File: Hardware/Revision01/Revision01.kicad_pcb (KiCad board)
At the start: 4 copper layers, 100 x 119.8 mm, 83 parts, among them J1 Battery connector, J2 StrainConn, J3 StrainConn, J4 StrainConn, J5 StrainConn, J6 StrainConn, J7 StrainConn, J8 StrainConn, J9 StrainConn, Q1 PMOS, Q2 NMOS, Q3 PMOS, SW1 StartStop_Push, SW2 ON/OFF_SW_SPST_LED, U1 NCP1117LPST50T3G, U2 NUCLEO-L476RG, U3 LP5813BDRRR, U4 MRF89XAM9AT-I/RM, U5 ICM-45605

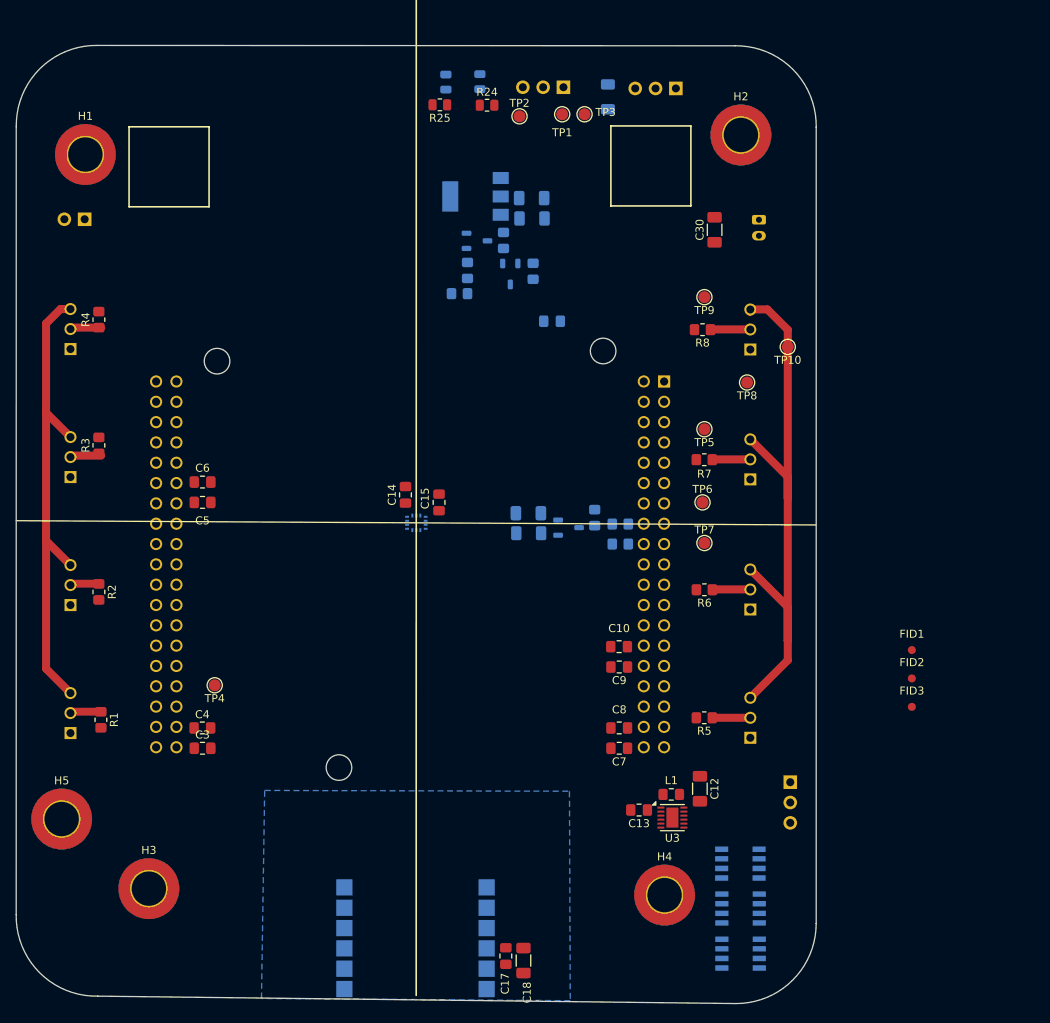
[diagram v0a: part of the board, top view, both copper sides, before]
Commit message: Added protection ciruitry and completed most of LAYOUT for PART A
 - Added SC protection against AMPLIFIER input circuitry
 -Completed PCB layout for STRAIN AMPLIFIER V1
 -Internal temperature sensor exists inside STM32
 -added schottky diodes to clamp over/undervoltage to protect ADC
 - Analog layer layout complete
 - Power circuitry layed out

Antenna has not been wired out
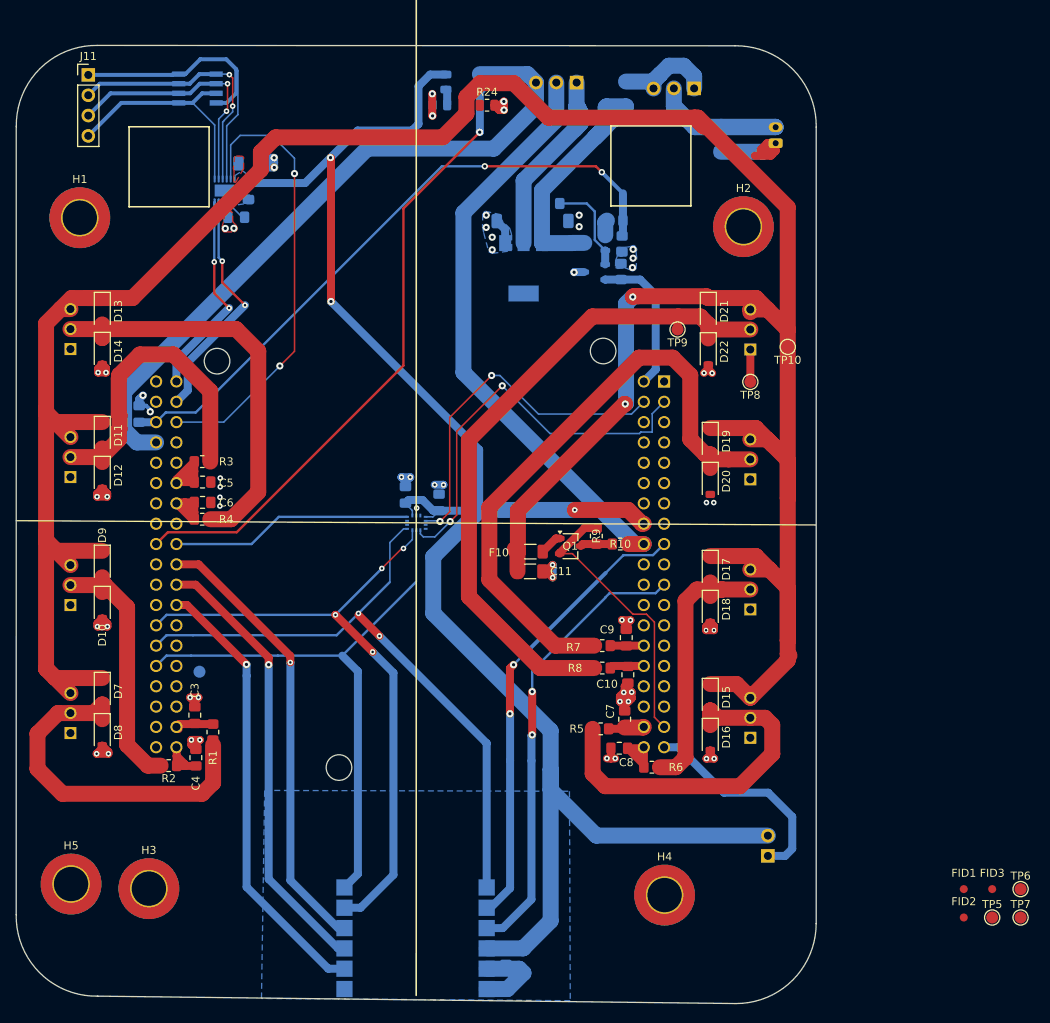
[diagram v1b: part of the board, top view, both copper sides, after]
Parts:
- removed D1: Indicication_RGB_Led, Connector_PinHeader_2.54mm:PinHeader_1x03_P2.54mm_Vertical
- removed D3, D4: RGBW_LED, RGBW:SOL120P540X160-8N
- removed R11: 0K +-1%, Resistor_SMD:R_0805_2012Metric_Pad1.20x1.40mm_HandSolder
- added D10: D_Schottky_Small, Diode_SMD:D_SOD-123, F.Cu at (121.8, 102.9)
- added D11: D_Schottky_Small, Diode_SMD:D_SOD-123, F.Cu at (121.8, 81.7)
- added D12: D_Schottky_Small, Diode_SMD:D_SOD-123, F.Cu at (121.8, 86.7)
- added D13: D_Schottky_Small, Diode_SMD:D_SOD-123, F.Cu at (121.8, 66.2)
- added D14: D_Schottky_Small, Diode_SMD:D_SOD-123, F.Cu at (121.8, 71.2)
- added D15: D_Schottky_Small, Diode_SMD:D_SOD-123, F.Cu at (197.8, 114.4)
- added D16: D_Schottky_Small, Diode_SMD:D_SOD-123, F.Cu at (197.8, 119.4)
- added D17: D_Schottky_Small, Diode_SMD:D_SOD-123, F.Cu at (197.8, 98.4)
- added D18: D_Schottky_Small, Diode_SMD:D_SOD-123, F.Cu at (197.8, 103.4)
- added D19: D_Schottky_Small, Diode_SMD:D_SOD-123, F.Cu at (197.8, 82.4)
- added D20: D_Schottky_Small, Diode_SMD:D_SOD-123, F.Cu at (197.8, 87.4)
- added D21: D_Schottky_Small, Diode_SMD:D_SOD-123, F.Cu at (197.5, 66.2)
- added D22: D_Schottky_Small, Diode_SMD:D_SOD-123, F.Cu at (197.5, 71.2)
- added D7: D_Schottky_Small, Diode_SMD:D_SOD-123, F.Cu at (121.8, 113.7)
- added D8: D_Schottky_Small, Diode_SMD:D_SOD-123, F.Cu at (121.8, 118.8)
- added D9: D_Schottky_Small, Diode_SMD:D_SOD-123, F.Cu at (121.8, 97.8)
- added J11: RGBW connector, Connector_PinHeader_2.54mm:PinHeader_1x04_P2.54mm_Vertical, F.Cu at (120.0, 36.6)
- C11, F10, Q1, R10, R9: moved to F.Cu
- C12, C13, C14, C15, C17, C18, C30, L1, R25, TP1, TP2, TP3, TP4, U3: moved to B.Cu
- moved D2 127.7 mm to (133.7, 38.3)
- moved SW1 116.7 mm to (205.0, 134.3), turned to 0 degrees
- moved U3 96.3 mm to (137.1, 51.1), turned to 90 degrees
- moved C12 96.2 mm to (140.4, 47.7), turned to 0 degrees
- moved L1 92.1 mm to (140.0, 51.2), turned to -90 degrees
- moved C13 89.6 mm to (138.5, 54.4)
- moved TP5 70.8 mm to (233.0, 142.0), turned to 0 degrees
- moved TP6 62.6 mm to (236.6, 138.4)
- moved TP7 61.3 mm to (236.6, 142.0)
- moved C16 52.9 mm to (126.4, 79.0), turned to 90 degrees
- moved R8 44.1 mm to (184.3, 110.8), turned to 0 degrees
- moved FID1 30.6 mm to (229.5, 138.4)
- moved FID2 30.6 mm to (229.5, 142.0)
- moved R4 28.1 mm to (134.3, 92.2), turned to 180 degrees
- moved R7 26.5 mm to (184.3, 108.0), turned to 0 degrees
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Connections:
- net Earth renamed GND
- C10 pad 1: /AIN1_6 -> /AIN1_5
- C16 pad 1: /BatteryV_AIN2 -> /PC5_AIN2_14_BATT_V
- C3 pad 1: /AIN1_8 -> /AIN1_7
- C4 pad 1: /AIN1_7 -> /AIN1_8
- C5 pad 1: /AIN1_11 -> /AIN1_10
- C6 pad 1: /AIN1_10 -> /AIN1_11
- C7 pad 1: /AIN1_1 -> /AIN1_2
- C8 pad 1: /AIN1_2 -> /AIN1_1
- C9 pad 1: /AIN1_5 -> /AIN1_6
- Q1 pad 3: Net-(Q1-S) -> unconnected-(Q1-S-Pad3)
- R1 pad 2: /AIN1_8 -> /AIN1_7
- R10 pad 1: Net-(Q1-S) -> unconnected-(Q1-S-Pad3)
- R2 pad 2: /AIN1_7 -> /AIN1_8
- R22 pad 1: /BatteryV_AIN2 -> /PC5_AIN2_14_BATT_V
- R23 pad 2: /BatteryV_AIN2 -> /PC5_AIN2_14_BATT_V
- R3 pad 2: /AIN1_11 -> /AIN1_10
- R4 pad 2: /AIN1_10 -> /AIN1_11
- R5 pad 2: /AIN1_1 -> /AIN1_2
- R6 pad 2: /AIN1_2 -> /AIN1_1
- R7 pad 2: /AIN1_5 -> /AIN1_6
- R8 pad 2: /AIN1_6 -> /AIN1_5
- R9 pad 2: Net-(Q1-S) -> unconnected-(Q1-S-Pad3)
- U2 pad CN10_17: unconnected-(U2B-PB6-PadCN10_17) -> /ICM_INT1_GPIO
- U2 pad CN10_18: unconnected-(U2B-PB11-PadCN10_18) -> /USB_5V_GPIO_EN
- U2 pad CN10_19: unconnected-(U2B-PC7-PadCN10_19) -> /ANT_IRQ0_GPIO
- U2 pad CN10_2: /ICM_INT1_GPIO -> unconnected-(U2B-PC8-PadCN10_2)
- U2 pad CN10_21: unconnected-(U2B-PA9-PadCN10_21) -> /ANT_CSCON_GPIO
- U2 pad CN10_23: unconnected-(U2B-PA8-PadCN10_23) -> /ANT_RESET_ANT_GPIO
- U2 pad CN10_4: /ICM_INT2_GPIO -> unconnected-(U2B-PC6-PadCN10_4)
- U2 pad CN10_6: /ICM_CS_GPIO -> /PC5_AIN2_14_BATT_V
- U2 pad CN7_17: unconnected-(U2A-PA15-PadCN7_17) -> /ANT_CSDATA_GPIO
- U2 pad CN7_2: unconnected-(U2A-PC11-PadCN7_2) -> /BatteryV_Div_Enable_GPIO
- U2 pad CN7_21: unconnected-(U2A-PB7-PadCN7_21) -> /ANT_IRQ1_GPIO
- U2 pad CN7_3: unconnected-(U2A-PC12-PadCN7_3) -> /ICM_CS_GPIO
- U2 pad CN7_35: unconnected-(U2A-PC2-PadCN7_35) -> /StrainV_Enable_GPIO
- U2 pad CN7_37: unconnected-(U2A-PC3-PadCN7_37) -> /STARTSTOP_GPIO
- U2 pad CN7_4: unconnected-(U2A-PD2-PadCN7_4) -> /ICM_INT2_GPIO
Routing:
- net /Application/+StrainV: track 135.5 -> 372.3 mm, vias 0 -> 2
- net +3.3V: track 0.00 -> 221.4 mm, vias 0 -> 3
- net GND: track 0.00 -> 108.4 mm, vias 0 -> 59
- net /PB15_SPI2_MOSI: track 0.00 -> 87.6 mm, vias 0 -> 4
- net +5V_USB: track 0.00 -> 86.1 mm
- net /Application/OpAmpOutput8: track 4.98 -> 86.4 mm
- net /PB14_SPI2_MISO: track 0.00 -> 81.2 mm, vias 0 -> 2
- net /PC5_AIN2_14_BATT_V: track 0.00 -> 80.5 mm, vias 0 -> 2
- net /USB_5V_GPIO_EN: track 0.00 -> 78.7 mm, vias 0 -> 1
- net /PB13_SPI2_SCK: track 0.00 -> 74.8 mm
- net +5V: track 0.00 -> 74.4 mm
- net /Application/OpAmpOutput7: track 4.77 -> 77.6 mm
- net /ANT_CSDATA_GPIO: track 0.00 -> 57.1 mm, vias 0 -> 2
- net /ANT_IRQ1_GPIO: track 0.00 -> 56.7 mm, vias 0 -> 2
- net /LP5813_EN_GPIO: track 0.00 -> 56.7 mm, vias 0 -> 2
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- added copper zone on B.Cu, net +3.3V
- added copper zone on F.Cu, net +3.3V
- added copper zone on B.Cu, net GND
- added copper zone on F.Cu, net GND
- added copper zone on B.Cu, net Net-(U3-SW)
- removed copper zone on B.Cu, net /I2C_SDA

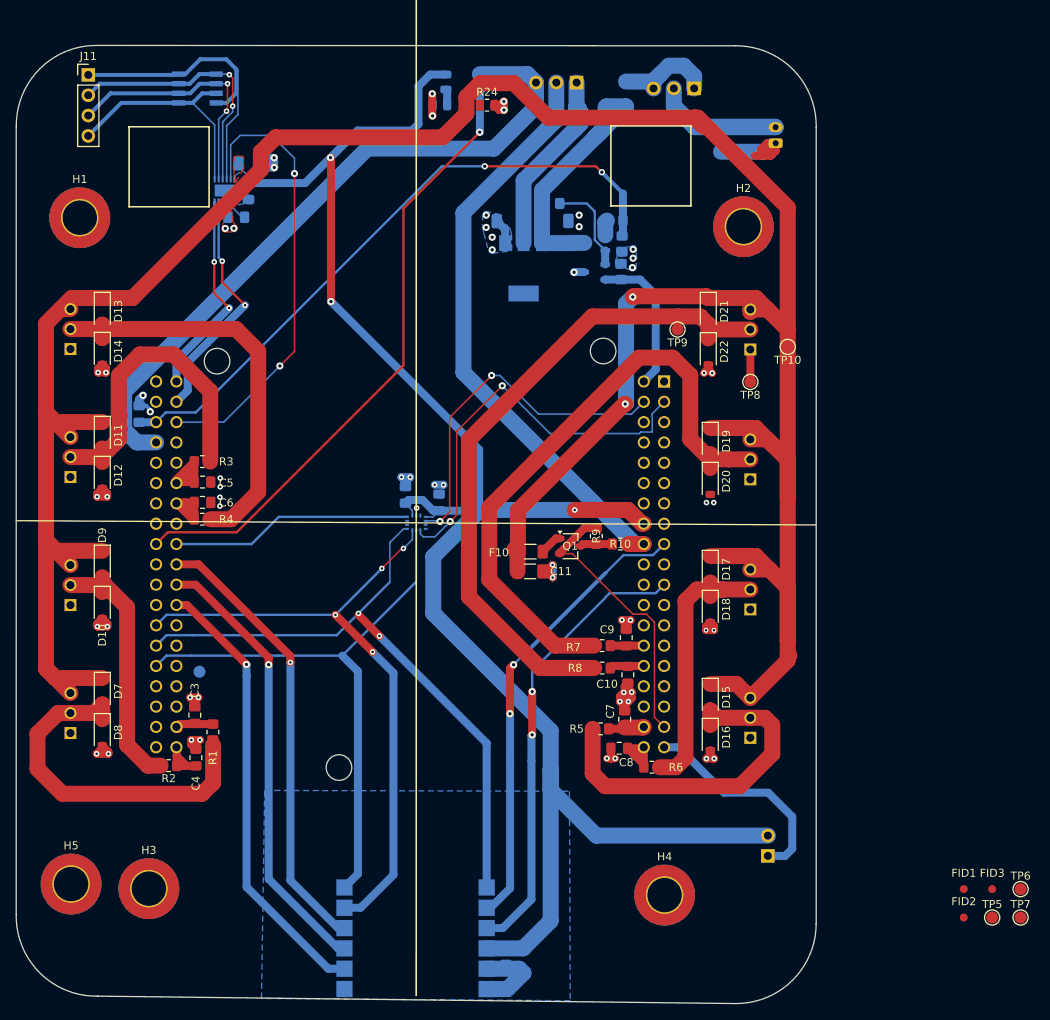
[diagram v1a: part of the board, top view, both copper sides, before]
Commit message: stimulated over/undervoltage protection and started correcting error
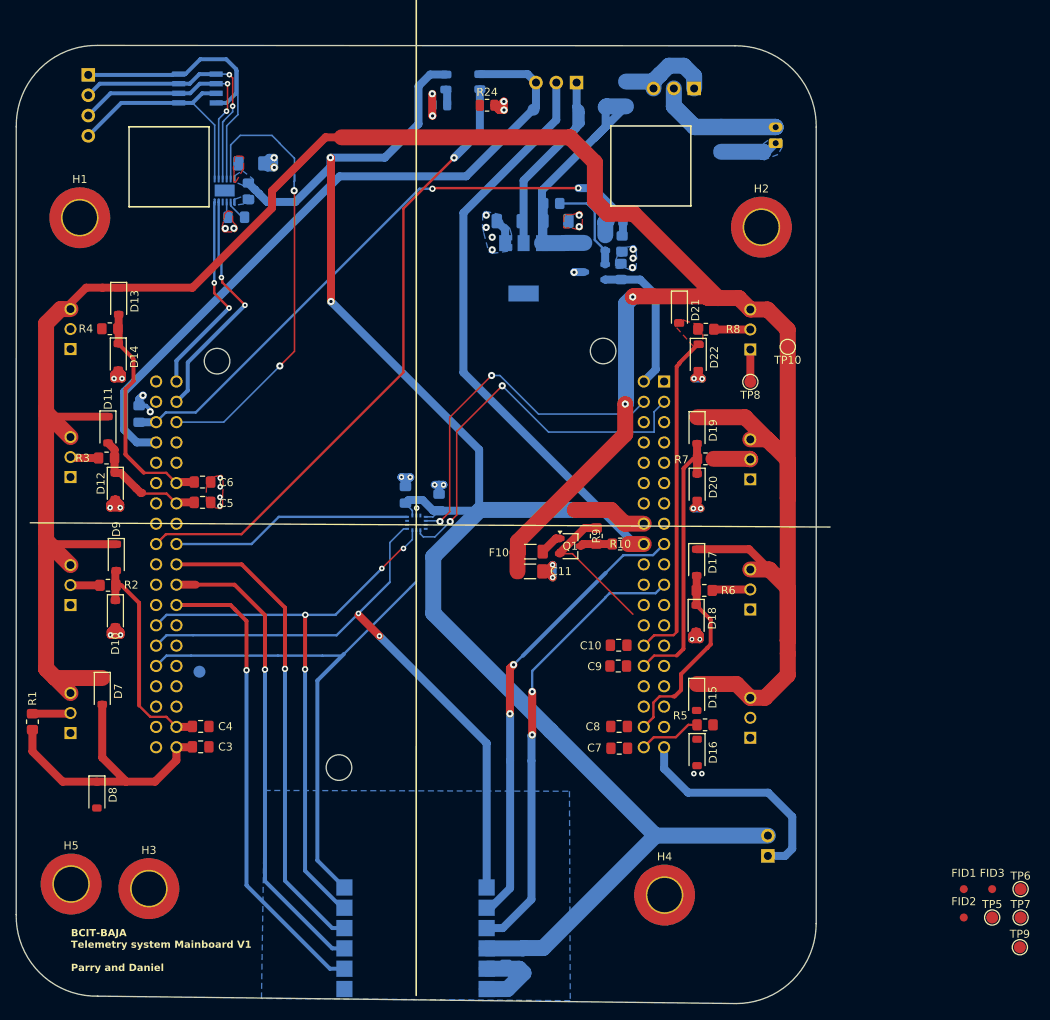
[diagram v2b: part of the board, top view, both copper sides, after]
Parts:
- J11: moved to B.Cu
- moved TP9 88.3 mm to (236.5, 145.7), turned to 0 degrees
- moved R8 44.3 mm to (197.2, 68.4), turned to 180 degrees
- moved R7 26.7 mm to (197.2, 84.6), turned to 180 degrees
- moved R4 26.5 mm to (122.7, 68.4), turned to 0 degrees
- moved R2 23.8 mm to (122.5, 100.4)
- moved R6 23.1 mm to (197.0, 101.1)
- moved R1 22.6 mm to (113.0, 117.5), turned to -90 degrees
- moved R5 13.1 mm to (197.1, 117.9), turned to 180 degrees
- moved R3 12.0 mm to (122.3, 84.5), turned to 0 degrees
- moved D8 7.83 mm to (121.1, 126.6)
- moved C3 4.03 mm to (134.1, 120.6), turned to 0 degrees
- moved C4 3.95 mm to (134.1, 118.1), turned to 0 degrees
- moved C10 3.86 mm to (186.3, 107.9), turned to 180 degrees
- moved C7 3.69 mm to (186.4, 120.8), turned to 180 degrees
- moved C9 3.69 mm to (186.3, 110.5), turned to 180 degrees
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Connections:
- C10 pad 1: /AIN1_5 -> /AIN1_6
- C3 pad 1: /AIN1_7 -> /AIN1_8
- C4 pad 1: /AIN1_8 -> /AIN1_7
- C5 pad 1: /AIN1_10 -> /AIN1_11
- C6 pad 1: /AIN1_11 -> /AIN1_10
- C7 pad 1: /AIN1_2 -> /AIN1_1
- C8 pad 1: /AIN1_1 -> /AIN1_2
- C9 pad 1: /AIN1_6 -> /AIN1_5
- D10 pad 1: /Application/OpAmpOutput2 -> /AIN1_7
- D11 pad 2: /Application/OpAmpOutput3 -> /AIN1_11
- D12 pad 1: /Application/OpAmpOutput3 -> /AIN1_11
- D13 pad 2: /Application/OpAmpOutput4 -> /AIN1_10
- D14 pad 1: /Application/OpAmpOutput4 -> /AIN1_10
- D15 pad 2: /Application/OpAmpOutput5 -> /AIN1_1
- D16 pad 1: /Application/OpAmpOutput5 -> /AIN1_1
- D17 pad 2: /Application/OpAmpOutput6 -> /AIN1_2
- D18 pad 1: /Application/OpAmpOutput6 -> /AIN1_2
- D19 pad 2: /Application/OpAmpOutput7 -> /AIN1_5
- D20 pad 1: /Application/OpAmpOutput7 -> /AIN1_5
- D21 pad 2: /Application/OpAmpOutput8 -> /AIN1_6
- D22 pad 1: /Application/OpAmpOutput8 -> /AIN1_6
- D7 pad 2: /Application/OpAmpOutput1 -> /AIN1_8
- D8 pad 1: /Application/OpAmpOutput1 -> /AIN1_8
- D9 pad 2: /Application/OpAmpOutput2 -> /AIN1_7
- R1 pad 2: /AIN1_7 -> /AIN1_8
- R2 pad 2: /AIN1_8 -> /AIN1_7
- R3 pad 2: /AIN1_10 -> /AIN1_11
- R4 pad 2: /AIN1_11 -> /AIN1_10
- R5 pad 2: /AIN1_2 -> /AIN1_1
- R6 pad 2: /AIN1_1 -> /AIN1_2
- R7 pad 2: /AIN1_6 -> /AIN1_5
- R8 pad 2: /AIN1_5 -> /AIN1_6
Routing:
- net /Application/OpAmpOutput8: track 86.4 -> 4.57 mm
- net /Application/OpAmpOutput7: track 77.6 -> 4.63 mm
- net /Application/OpAmpOutput4: track 52.6 -> 0.00 mm
- net /Application/OpAmpOutput5: track 46.0 -> 0.00 mm
- net /Application/OpAmpOutput1: track 44.6 -> 5.03 mm
- net /AIN1_6: track 4.19 -> 41.9 mm
- net /Application/OpAmpOutput3: track 40.0 -> 3.57 mm
- net GND: track 108.4 -> 73.6 mm, vias 59 -> 45
- net /AIN1_8: track 6.47 -> 39.8 mm
- net /AIN1_5: track 4.30 -> 35.6 mm
- net /Application/OpAmpOutput6: track 35.3 -> 4.81 mm
- net /Application/OpAmpOutput2: track 32.6 -> 3.70 mm
- net /AIN1_7: track 5.09 -> 28.2 mm
- net /AIN1_2: track 4.49 -> 24.3 mm
- net /AIN1_10: track 10.4 -> 28.9 mm
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- added copper zone on F.Cu, net /AIN1_5
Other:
- board text added: "BCIT-BAJA Telemetry system Mainboard V1 Parry and Daniel"
